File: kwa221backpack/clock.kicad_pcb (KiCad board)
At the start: 2 copper layers, 58.4 x 81.3 mm, 5 parts, among them P1 CONN_01X10, P2 CONN_01X10, U1 TLC5940NT

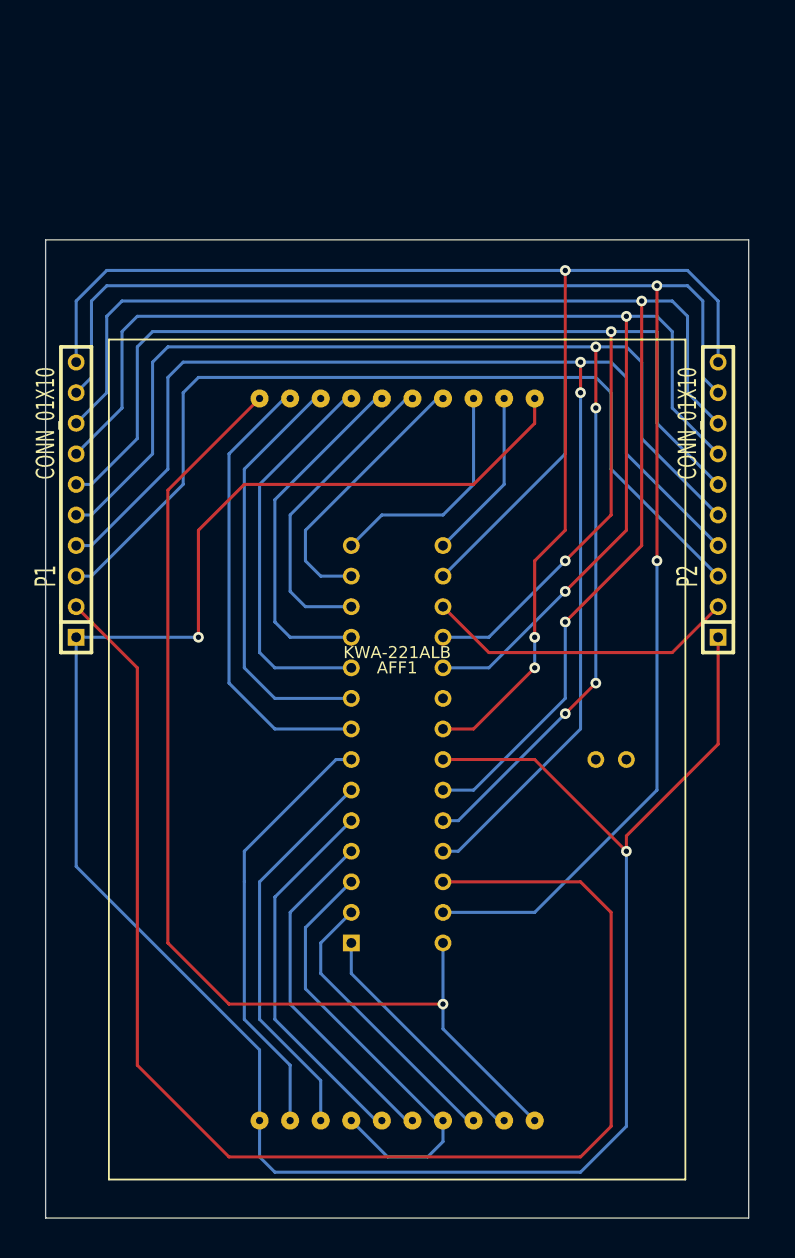
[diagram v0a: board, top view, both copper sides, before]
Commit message: Re-order pins on header to simplify chip routing
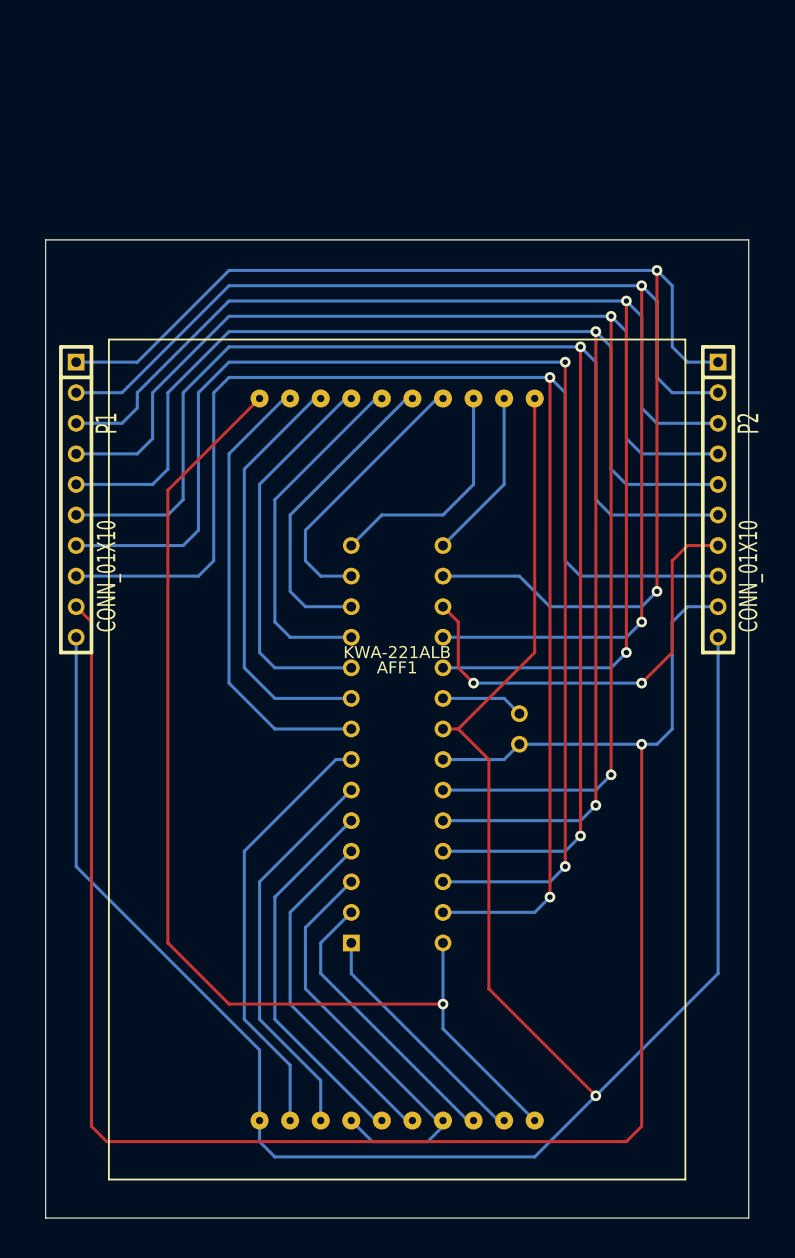
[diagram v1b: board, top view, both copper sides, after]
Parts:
- moved R1 8.03 mm to (82.5, 71.1), turned to 270 degrees
- turned P1 to 270 degrees
- turned P2 to 270 degrees
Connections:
- P1 pad 1: VCC -> /XERR
- P1 pad 10: GND -> VCC
- P1 pad 2: /SIN -> /GSCLK
- P1 pad 3: /XERR -> /DCPRG
- P1 pad 4: /SCLK -> /BLANK
- P1 pad 6: /GSCLK -> /SCLK
- P1 pad 7: /DCPRG -> /SIN
- P1 pad 8: /BLANK -> /VPRG
- P1 pad 9: /VPRG -> GND
- P2 pad 1: VCC -> /XERR
- P2 pad 10: GND -> VCC
- P2 pad 2: /SOUT -> /GSCLK
- P2 pad 3: /XERR -> /DCPRG
- P2 pad 4: /SCLK -> /BLANK
- P2 pad 6: /GSCLK -> /SCLK
- P2 pad 7: /DCPRG -> /SOUT
- P2 pad 8: /BLANK -> /VPRG
- P2 pad 9: /VPRG -> GND
- R1 pad 2: (no net) -> GND
- U1 pad 21: GND -> VCC
- U1 pad 22: VCC -> GND
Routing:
- net GND: track 109.4 -> 155.6 mm, vias 4 -> 1
- net /XERR: track 95.9 -> 108.7 mm, vias 0 -> 2
- net /SOUT: track 26.0 -> 36.9 mm, vias 1 -> 2
- net /SIN: track 116.6 -> 106.2 mm, vias 1 -> 2
- net VCC: track 197.0 -> 187.7 mm, vias 2 -> 1
- net /SCLK: track 120.3 -> 129.4 mm
- net /XLAT: track 118.5 -> 126.1 mm, vias 4 -> 2
- net IREF: track 0.00 -> 6.88 mm
- net /BLANK: track 118.2 -> 122.8 mm
- net /VPRG: track 132.0 -> 136.0 mm
- net /DCPRG: track 108.0 -> 111.9 mm
- net /GSCLK: track 106.2 -> 109.4 mm
- net /D3: track 37.6 -> 35.8 mm
- net /D5: vias 1 -> 0
- net /D2: vias 1 -> 0
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
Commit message: Moving the headers up -- not sure I like this
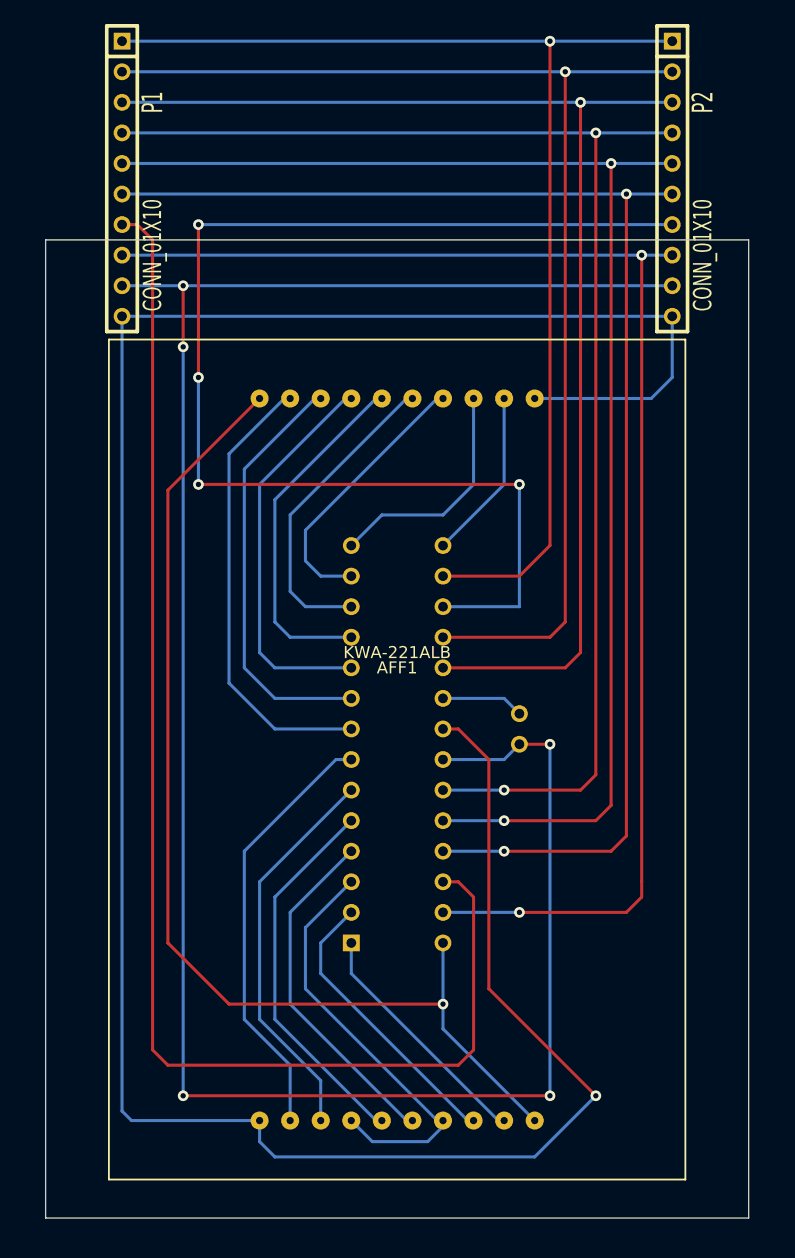
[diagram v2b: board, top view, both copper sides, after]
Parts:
- moved P1 26.9 mm to (49.5, 25.4)
- moved P2 26.9 mm to (95.2, 25.4)
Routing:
- net /SOUT: track 36.9 -> 104.1 mm, vias 2 -> 4
- net GND: track 155.6 -> 182.1 mm, vias 1 -> 5
- net VCC: track 187.7 -> 209.6 mm
- net /VPRG: track 136.0 -> 116.1 mm
- net /SCLK: track 129.4 -> 114.8 mm
- net /XLAT: track 126.1 -> 113.6 mm
- net /XERR: track 108.7 -> 97.6 mm, vias 2 -> 1
- net /BLANK: track 122.8 -> 112.3 mm
- net /DCPRG: track 111.9 -> 103.4 mm, vias 2 -> 1
- net /SIN: track 106.2 -> 113.9 mm, vias 2 -> 0
- net /GSCLK: track 109.4 -> 102.1 mm, vias 2 -> 1

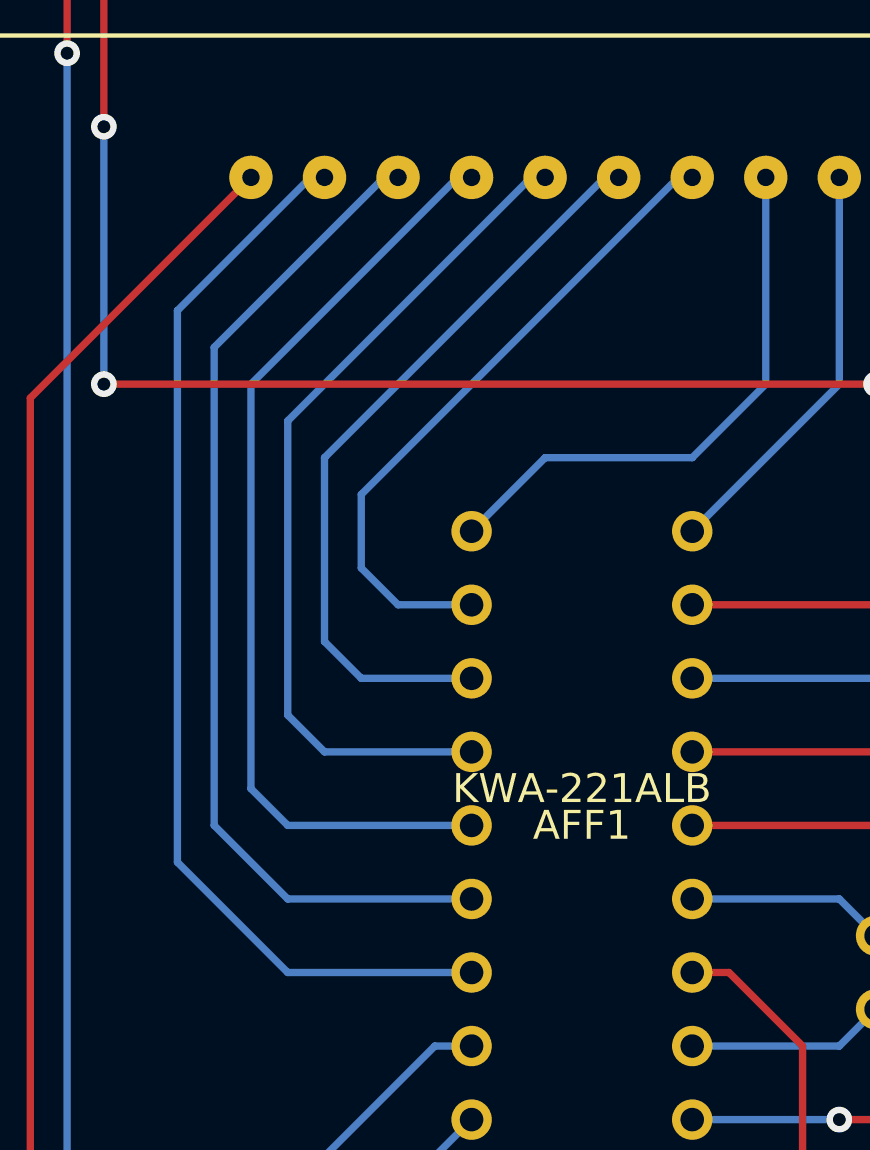
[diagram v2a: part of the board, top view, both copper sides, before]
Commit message: Moving the top traces closer to the IC
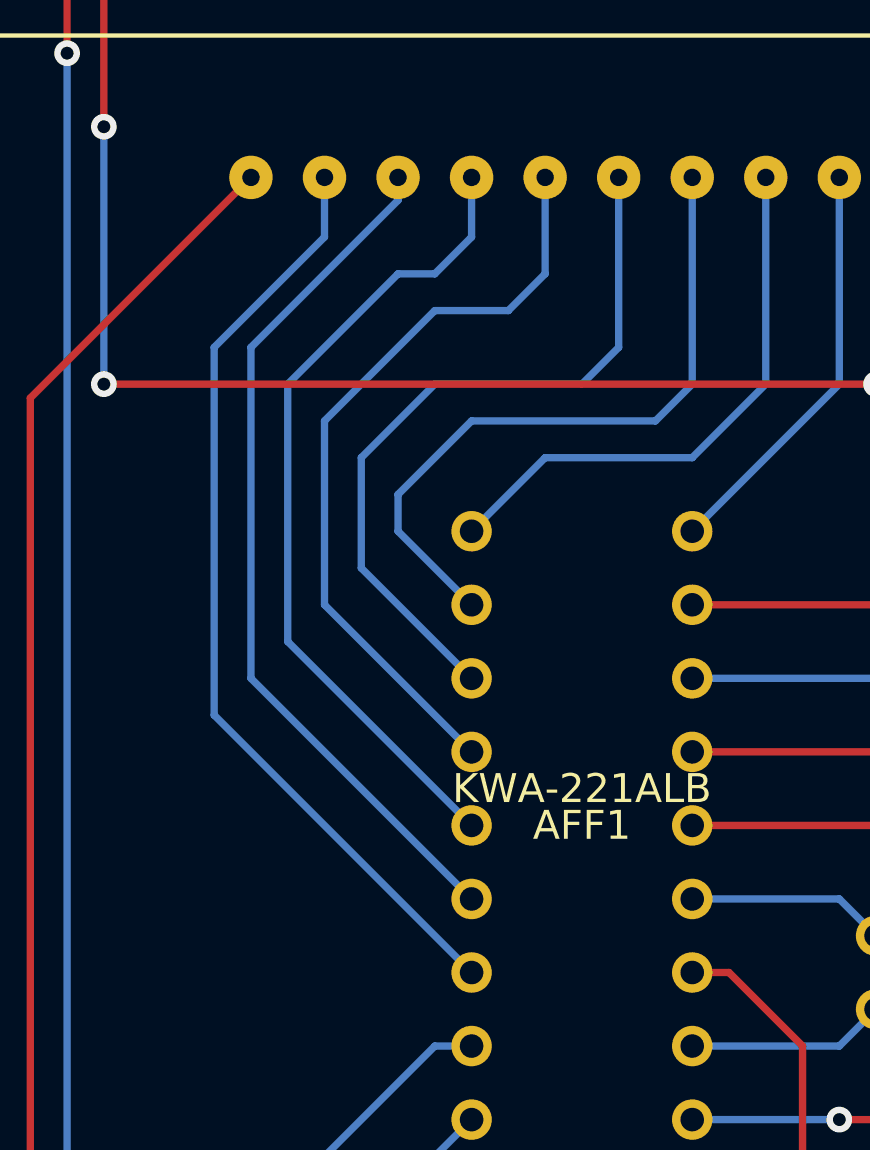
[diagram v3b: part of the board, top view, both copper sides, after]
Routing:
- net /D9: track 35.2 -> 30.2 mm
- net /D8: track 37.8 -> 32.7 mm
- net /D10: track 32.7 -> 28.4 mm
- net /D11: track 29.4 -> 26.6 mm
- net /D13: track 22.8 -> 23.7 mm
- net /D12: track 26.1 -> 25.5 mm
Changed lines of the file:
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@@
     (links 42)
     (no_connects 0)
-    (area 43.129999 30.429999 102.87127 111.810001)
+    (area 43.129999 12.293599 101.650001 111.810001)
     (thickness 1.6)
     (drawings 4)
-    (tracks 178)
+    (tracks 180)
     (zones 0)
     (modules 5)
@@
   (segment (start 68.58 91.44) (end 68.58 88.9) (width 0.254) (layer B.Cu) (net 3) (status 20))
   (segment (start 80.8 103.66) (end 68.58 91.44) (width 0.254) (layer B.Cu) (net 3) (status 10))
-  (segment (start 68.58 43.66) (end 68.1 43.66) (width 0.254) (layer B.Cu) (net 4) (status 30))
-  (segment (start 62.23 66.04) (end 68.58 66.04) (width 0.254) (layer B.Cu) (net 4) (status 20))
-  (segment (start 60.96 64.77) (end 62.23 66.04) (width 0.254) (layer B.Cu) (net 4))
-  (segment (start 60.96 50.8) (end 60.96 64.77) (width 0.254) (layer B.Cu) (net 4))
-  (segment (start 68.1 43.66) (end 60.96 50.8) (width 0.254) (layer B.Cu) (net 4) (status 10))
-  (segment (start 71.12 43.66) (end 70.64 43.66) (width 0.254) (layer B.Cu) (net 5) (status 30))
-  (segment (start 63.5 63.5) (end 68.58 63.5) (width 0.254) (layer B.Cu) (net 5) (status 20))
-  (segment (start 62.23 62.23) (end 63.5 63.5) (width 0.254) (layer B.Cu) (net 5))
-  (segment (start 62.23 52.07) (end 62.23 62.23) (width 0.254) (layer B.Cu) (net 5))
-  (segment (start 70.64 43.66) (end 62.23 52.07) (width 0.254) (layer B.Cu) (net 5) (status 10))
-  (segment (start 73.66 43.66) (end 73.18 43.66) (width 0.254) (layer B.Cu) (net 6) (status 30))
-  (segment (start 64.77 60.96) (end 68.58 60.96) (width 0.254) (layer B.Cu) (net 6) (status 20))
-  (segment (start 63.5 59.69) (end 64.77 60.96) (width 0.254) (layer B.Cu) (net 6))
-  (segment (start 63.5 53.34) (end 63.5 59.69) (width 0.254) (layer B.Cu) (net 6))
-  (segment (start 73.18 43.66) (end 63.5 53.34) (width 0.254) (layer B.Cu) (net 6) (status 10))
-  (segment (start 76.2 43.66) (end 75.72 43.66) (width 0.254) (layer B.Cu) (net 7) (status 30))
-  (segment (start 66.04 58.42) (end 68.58 58.42) (width 0.254) (layer B.Cu) (net 7) (status 20))
-  (segment (start 64.77 57.15) (end 66.04 58.42) (width 0.254) (layer B.Cu) (net 7))
-  (segment (start 64.77 54.61) (end 64.77 57.15) (width 0.254) (layer B.Cu) (net 7))
-  (segment (start 75.72 43.66) (end 64.77 54.61) (width 0.254) (layer B.Cu) (net 7) (status 10))
+  (segment (start 68.58 66.04) (end 62.23 59.69) (width 0.254) (layer B.Cu) (net 4) (status 400000))
+  (segment (start 68.58 45.72) (end 68.58 43.66) (width 0.254) (layer B.Cu) (net 4) (status 800000))
+  (segment (start 67.31 46.99) (end 68.58 45.72) (width 0.254) (layer B.Cu) (net 4))
+  (segment (start 66.04 46.99) (end 67.31 46.99) (width 0.254) (layer B.Cu) (net 4))
+  (segment (start 62.23 50.8) (end 66.04 46.99) (width 0.254) (layer B.Cu) (net 4))
+  (segment (start 62.23 59.69) (end 62.23 50.8) (width 0.254) (layer B.Cu) (net 4))
+  (segment (start 68.58 63.5) (end 63.5 58.42) (width 0.254) (layer B.Cu) (net 5) (status 400000))
+  (segment (start 71.12 46.99) (end 71.12 43.66) (width 0.254) (layer B.Cu) (net 5) (status 800000))
+  (segment (start 69.85 48.26) (end 71.12 46.99) (width 0.254) (layer B.Cu) (net 5))
+  (segment (start 67.31 48.26) (end 69.85 48.26) (width 0.254) (layer B.Cu) (net 5))
+  (segment (start 63.5 52.07) (end 67.31 48.26) (width 0.254) (layer B.Cu) (net 5))
+  (segment (start 63.5 58.42) (end 63.5 52.07) (width 0.254) (layer B.Cu) (net 5))
+  (segment (start 68.58 60.96) (end 64.77 57.15) (width 0.254) (layer B.Cu) (net 6))
+  (segment (start 73.66 49.53) (end 73.66 43.66) (width 0.254) (layer B.Cu) (net 6))
+  (segment (start 72.39 50.8) (end 73.66 49.53) (width 0.254) (layer B.Cu) (net 6))
+  (segment (start 67.31 50.8) (end 72.39 50.8) (width 0.254) (layer B.Cu) (net 6))
+  (segment (start 64.77 53.34) (end 67.31 50.8) (width 0.254) (layer B.Cu) (net 6))
+  (segment (start 64.77 57.15) (end 64.77 53.34) (width 0.254) (layer B.Cu) (net 6))
+  (segment (start 68.58 58.42) (end 66.04 55.88) (width 0.254) (layer B.Cu) (net 7))
+  (segment (start 76.2 50.8) (end 76.2 43.66) (width 0.254) (layer B.Cu) (net 7))
+  (segment (start 74.93 52.07) (end 76.2 50.8) (width 0.254) (layer B.Cu) (net 7))
+  (segment (start 68.58 52.07) (end 74.93 52.07) (width 0.254) (layer B.Cu) (net 7))
+  (segment (start 66.04 54.61) (end 68.58 52.07) (width 0.254) (layer B.Cu) (net 7))
+  (segment (start 66.04 55.88) (end 66.04 54.61) (width 0.254) (layer B.Cu) (net 7))
   (segment (start 78.74 43.66) (end 78.74 50.8) (width 0.254) (layer B.Cu) (net 8) (status 10))
   (segment (start 71.12 53.34) (end 68.58 55.88) (width 0.254) (layer B.Cu) (net 8) (status 20))
@@
   (segment (start 59.69 95.25) (end 59.69 81.28) (width 0.254) (layer B.Cu) (net 15))
   (segment (start 63.5 99.06) (end 59.69 95.25) (width 0.254) (layer B.Cu) (net 15))
-  (segment (start 63.5 43.66) (end 63.02 43.66) (width 0.254) (layer B.Cu) (net 16) (status 30))
-  (segment (start 62.23 71.12) (end 68.58 71.12) (width 0.254) (layer B.Cu) (net 16) (status 20))
-  (segment (start 58.42 67.31) (end 62.23 71.12) (width 0.254) (layer B.Cu) (net 16))
-  (segment (start 58.42 48.26) (end 58.42 67.31) (width 0.254) (layer B.Cu) (net 16))
-  (segment (start 63.02 43.66) (end 58.42 48.26) (width 0.254) (layer B.Cu) (net 16) (status 10))
-  (segment (start 66.04 43.66) (end 65.56 43.66) (width 0.254) (layer B.Cu) (net 17) (status 30))
-  (segment (start 62.23 68.58) (end 68.58 68.58) (width 0.254) (layer B.Cu) (net 17) (status 20))
-  (segment (start 59.69 66.04) (end 62.23 68.58) (width 0.254) (layer B.Cu) (net 17))
-  (segment (start 59.69 49.53) (end 59.69 66.04) (width 0.254) (layer B.Cu) (net 17))
-  (segment (start 65.56 43.66) (end 59.69 49.53) (width 0.254) (layer B.Cu) (net 17) (status 10))
+  (segment (start 68.58 71.12) (end 59.69 62.23) (width 0.254) (layer B.Cu) (net 16) (status 400000))
+  (segment (start 63.5 45.72) (end 63.5 43.66) (width 0.254) (layer B.Cu) (net 16) (status 800000))
+  (segment (start 59.69 49.53) (end 63.5 45.72) (width 0.254) (layer B.Cu) (net 16))
+  (segment (start 59.69 62.23) (end 59.69 49.53) (width 0.254) (layer B.Cu) (net 16))
+  (segment (start 68.58 68.58) (end 60.96 60.96) (width 0.254) (layer B.Cu) (net 17) (status 400000))
+  (segment (start 66.04 44.45) (end 66.04 43.66) (width 0.254) (layer B.Cu) (net 17) (status 800000))
+  (segment (start 60.96 49.53) (end 66.04 44.45) (width 0.254) (layer B.Cu) (net 17))
+  (segment (start 60.96 60.96) (end 60.96 49.53) (width 0.254) (layer B.Cu) (net 17))
   (via (at 87.63 19.05) (size 0.889) (layers F.Cu B.Cu) (net 18))
   (segment (start 76.2 66.04) (end 86.36 66.04) (width 0.254) (layer F.Cu) (net 18) (status 10))
@@
   (segment (start 49.53 26.67) (end 91.44 26.67) (width 0.254) (layer B.Cu) (net 20) (status 10))
   (segment (start 91.44 26.67) (end 95.25 26.67) (width 0.254) (layer B.Cu) (net 20) (status 20))
-  (segment (start 49.53 29.21) (end 50.8 29.21) (width 0.254) (layer F.Cu) (net 21) (status 400000))
-  (segment (start 77.47 83.82) (end 76.2 83.82) (width 0.254) (layer F.Cu) (net 21) (status 800000))
+  (segment (start 49.53 29.21) (end 50.8 29.21) (width 0.254) (layer F.Cu) (net 21))
+  (segment (start 77.47 83.82) (end 76.2 83.82) (width 0.254) (layer F.Cu) (net 21))
   (segment (start 78.74 85.09) (end 77.47 83.82) (width 0.254) (layer F.Cu) (net 21))
   (segment (start 78.74 97.79) (end 78.74 85.09) (width 0.254) (layer F.Cu) (net 21))
@@
   (segment (start 52.07 30.48) (end 52.07 97.79) (width 0.254) (layer F.Cu) (net 21))
   (segment (start 50.8 29.21) (end 52.07 30.48) (width 0.254) (layer F.Cu) (net 21))
-  (segment (start 76.2 60.96) (end 82.55 60.96) (width 0.254) (layer B.Cu) (net 22) (status 400000))
-  (segment (start 55.88 29.21) (end 95.25 29.21) (width 0.254) (layer B.Cu) (net 22) (status 800000))
+  (segment (start 76.2 60.96) (end 82.55 60.96) (width 0.254) (layer B.Cu) (net 22))
+  (segment (start 55.88 29.21) (end 95.25 29.21) (width 0.254) (layer B.Cu) (net 22))
   (via (at 55.88 29.21) (size 0.889) (layers F.Cu B.Cu) (net 22))
   (segment (start 55.88 41.91) (end 55.88 29.21) (width 0.254) (layer F.Cu) (net 22))
@@
   (segment (start 82.55 60.96) (end 82.55 50.8) (width 0.254) (layer B.Cu) (net 22))
   (via (at 92.71 31.75) (size 0.889) (layers F.Cu B.Cu) (net 23))
-  (segment (start 76.2 86.36) (end 82.55 86.36) (width 0.254) (layer B.Cu) (net 23) (status 400000))
+  (segment (start 76.2 86.36) (end 82.55 86.36) (width 0.254) (layer B.Cu) (net 23))
   (via (at 82.55 86.36) (size 0.889) (layers F.Cu B.Cu) (net 23))
   (segment (start 91.44 86.36) (end 82.55 86.36) (width 0.254) (layer F.Cu) (net 23))
@@
   (segment (start 90.17 24.13) (end 95.25 24.13) (width 0.254) (layer B.Cu) (net 25) (status 20))
   (via (at 54.61 34.29) (size 0.889) (layers F.Cu B.Cu) (net 26))
-  (segment (start 82.55 72.39) (end 85.09 72.39) (width 0.254) (layer F.Cu) (net 26) (status 400000))
+  (segment (start 82.55 72.39) (end 85.09 72.39) (width 0.254) (layer F.Cu) (net 26))
   (via (at 85.09 72.39) (size 0.889) (layers F.Cu B.Cu) (net 26))
   (segment (start 85.09 101.6) (end 85.09 72.39) (width 0.254) (layer B.Cu) (net 26))
@@
   (segment (start 76.2 68.58) (end 81.28 68.58) (width 0.254) (layer B.Cu) (net 27) (status 10))
   (segment (start 81.28 68.58) (end 82.55 69.85) (width 0.254) (layer B.Cu) (net 27) (status 20))
-  (segment (start 49.53 36.83) (end 49.53 102.87) (width 0.254) (layer B.Cu) (net 28) (status 400000))
-  (segment (start 50.32 103.66) (end 60.96 103.66) (width 0.254) (layer B.Cu) (net 28) (status 800000))
+  (segment (start 49.53 36.83) (end 49.53 102.87) (width 0.254) (layer B.Cu) (net 28))
+  (segment (start 50.32 103.66) (end 60.96 103.66) (width 0.254) (layer B.Cu) (net 28))
   (segment (start 49.53 102.87) (end 50.32 103.66) (width 0.254) (layer B.Cu) (net 28))
   (segment (start 83.82 43.66) (end 93.5 43.66) (width 0.254) (layer B.Cu) (net 28) (status 10))
